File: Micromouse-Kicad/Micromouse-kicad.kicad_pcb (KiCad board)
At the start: 2 copper layers, 101 parts, among them J1 SWD, J2 USB_B_Micro, J3 UARTBTH, J4 Batería, J5 VL6180x, J6 MotorEncodL, J7 MotorEncodR, Q1 BS170, Q2 BS170, Q3 BS170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

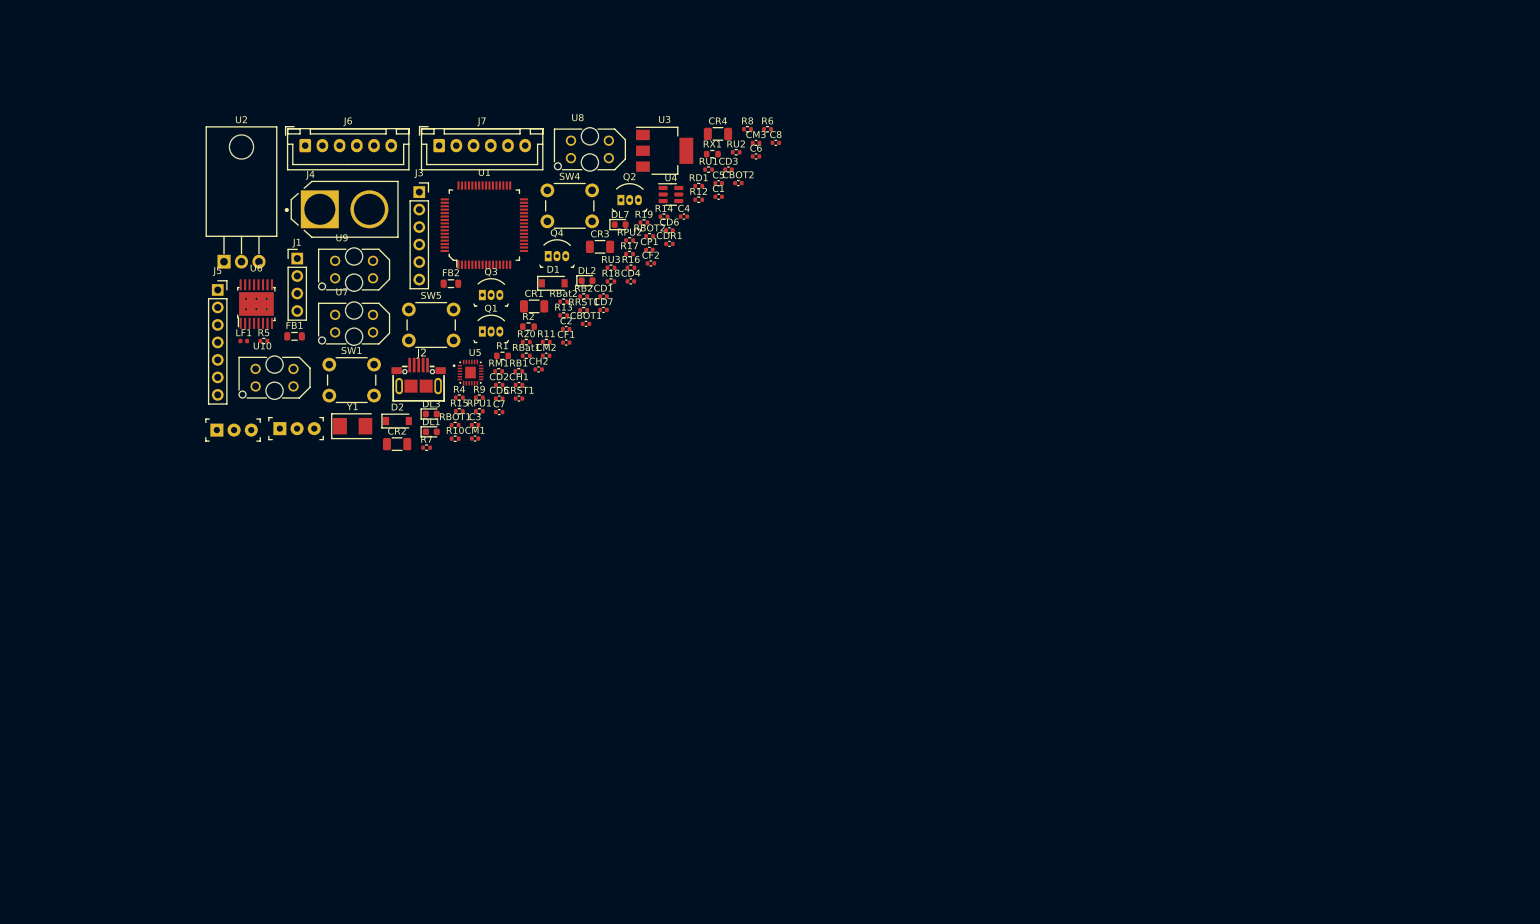
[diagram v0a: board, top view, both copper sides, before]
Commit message: Avance PCB - Forma y motores
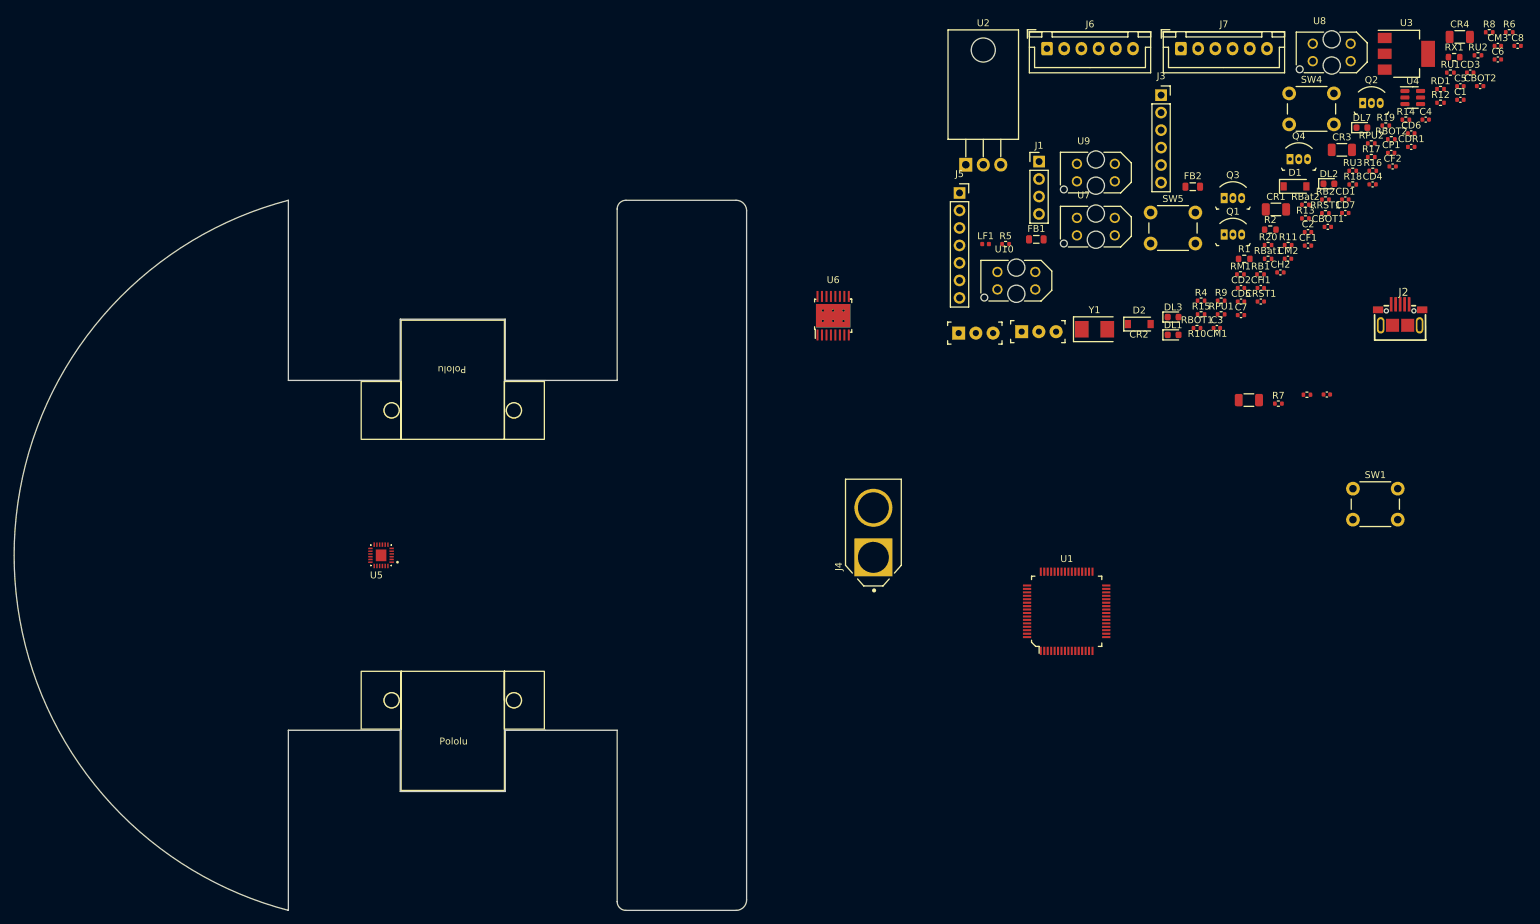
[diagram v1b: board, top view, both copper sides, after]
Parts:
- added Pololu: MotorHolder, custom:MotorHolder, F.Cu at (145.2, 119.5)
- added Pololu: MotorHolder, custom:MotorHolder, F.Cu at (160.2, 85.8)
- moved SW1 149.8 mm to (283.4, 92.9)
- moved J2 142.8 mm to (290.2, 67.7)
- moved CM1 123.9 mm to (279.6, 79.3)
- moved CR2 123.9 mm to (268.3, 80.1)
- moved R7 123.9 mm to (272.6, 80.6)
- moved R10 123.9 mm to (276.7, 79.3)
- moved D1 108.6 mm to (275.0, 49.0)
- moved R11 108.6 mm to (274.0, 57.6)
- moved C1 108.6 mm to (299.0, 36.5)
- moved C2 108.6 mm to (276.9, 55.7)
- moved C3 108.6 mm to (263.6, 69.6)
- moved C5 108.6 mm to (299.0, 34.5)
- moved C6 108.6 mm to (304.4, 30.6)
- moved C7 108.6 mm to (267.1, 67.7)
- moved C8 108.6 mm to (307.3, 28.6)
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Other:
- board outline added: 106.4 x 103.1 mm

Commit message: Motores routeados
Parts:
- RU2, RU3: footprint Resistor_SMD:R_0402_1005Metric -> Resistor_SMD:R_0603_1608Metric
- U2: value LM7805_TO220 -> AMS1117-5.0; footprint Package_TO_SOT_THT:TO-220-3_Horizontal_TabDown -> Package_TO_SOT_SMD:SOT-223-3_TabPin2
- moved C8 205.6 mm to (110.2, 87.4)
- moved C6 204.3 mm to (108.2, 87.4)
- moved R18 187.5 mm to (98.6, 80.8)
- moved R14 186.2 mm to (110.2, 83.8), turned to 180 degrees
- moved CR4 184.4 mm to (129.1, 99.3)
- moved U3 183.2 mm to (122.9, 102.2), turned to 90 degrees
- moved U7 181.2 mm to (67.3, 84.8), turned to 90 degrees
- moved R16 180.1 mm to (110.2, 85.1), turned to 180 degrees
- moved R1 179.2 mm to (90.1, 34.9)
- moved R11 179.2 mm to (96.4, 32.9)
- moved R12 179.2 mm to (118.6, 12.3)
- moved R13 179.2 mm to (98.9, 29.1)
- moved C1 179.2 mm to (121.4, 11.8)
- moved C2 179.2 mm to (99.3, 31.0)
- moved C3 179.2 mm to (86.1, 45.0)
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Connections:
- U2 pad 1: Net-(CR1-Pad1) -> GND
- U2 pad 2: GND -> +5V
- U2 pad 3: +5V -> Net-(CR1-Pad1)
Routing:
- net GND: track 0.00 -> 75.9 mm, vias 0 -> 29
- net TIM1_CH1: track 0.00 -> 44.5 mm, vias 0 -> 2
- net TIM1_CH2: track 0.00 -> 43.2 mm, vias 0 -> 2
- net TIM8_CH1: track 0.00 -> 40.5 mm, vias 0 -> 2
- net TIM8_CH2: track 0.00 -> 35.5 mm, vias 0 -> 2
- net MR1: track 0.00 -> 32.4 mm, vias 0 -> 2
- net MR2: track 0.00 -> 28.9 mm, vias 0 -> 2
- net +3.3V: track 0.00 -> 26.7 mm, vias 0 -> 9
- net ML1: track 0.00 -> 24.8 mm, vias 0 -> 2
- net ML2: track 0.00 -> 24.3 mm, vias 0 -> 2
- net +5V: track 0.00 -> 23.0 mm, vias 0 -> 4
- net OutMR2: track 0.00 -> 21.9 mm
- net /USB_STM32_D+: track 0.00 -> 19.1 mm
- net OutML2: track 0.00 -> 19.1 mm
- net /USB_STM32_D-: track 0.00 -> 17.3 mm
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- added copper zone on In2.Cu, net +3.3V
- added copper zone on In2.Cu, net +5V
- added copper zone on In1.Cu, net GND
- added copper zone on In2.Cu, net VCC
- added copper zone on In2.Cu, net Vdrive
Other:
- copper layers 2 -> 4

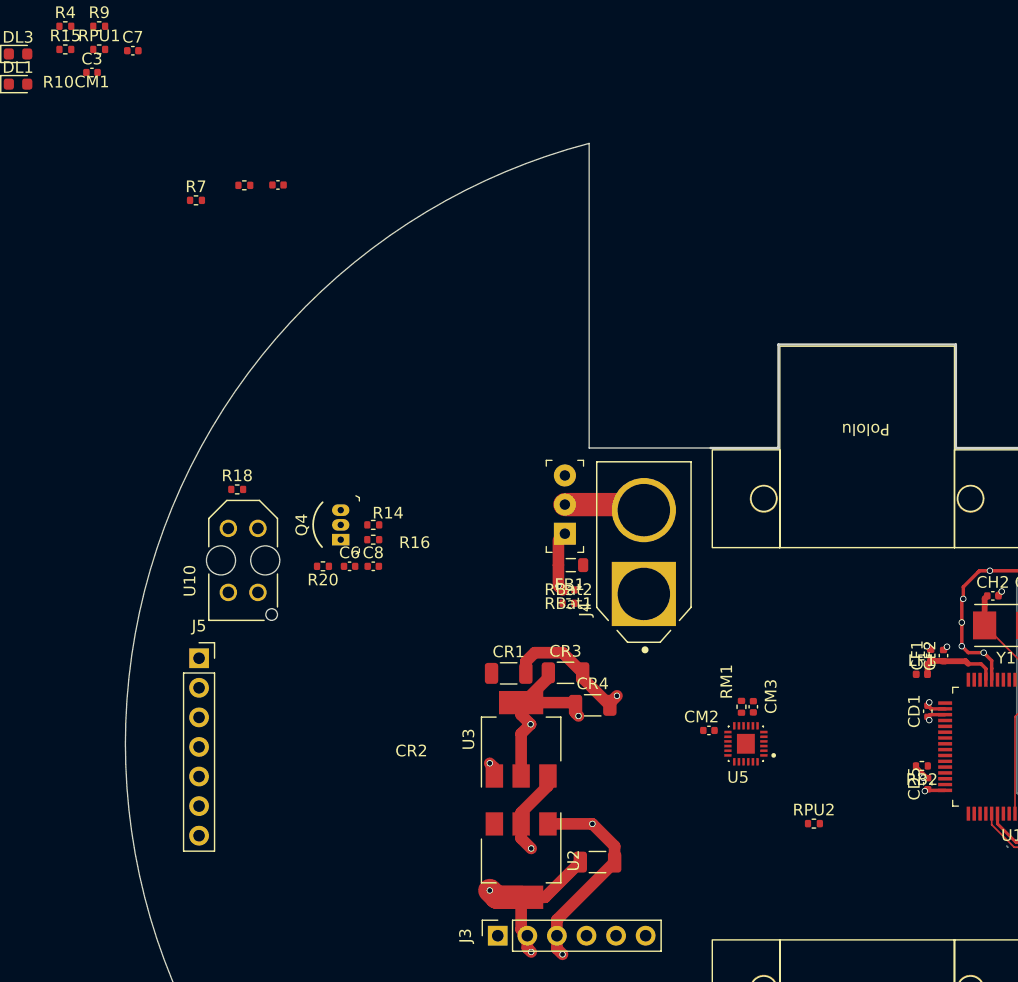
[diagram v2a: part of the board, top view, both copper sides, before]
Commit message: MPU6500 routeado
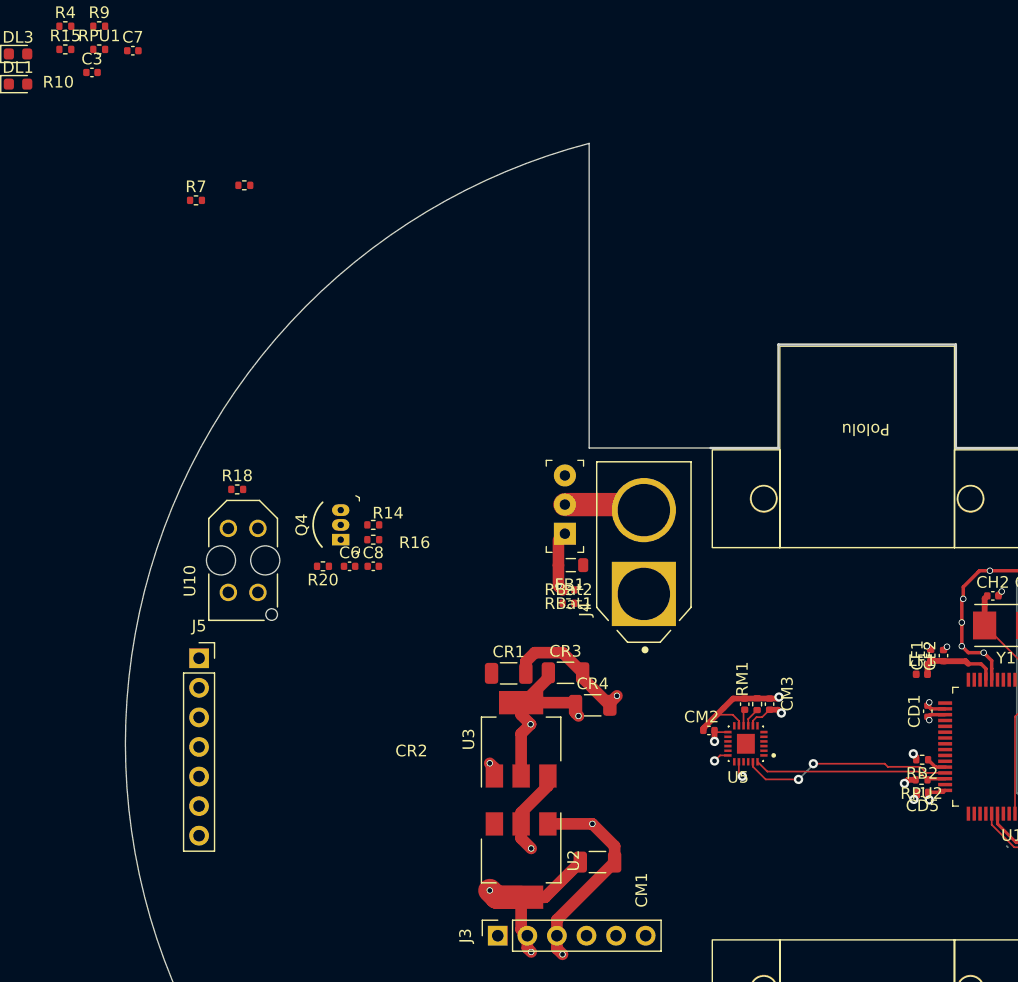
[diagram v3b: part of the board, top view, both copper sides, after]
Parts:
- moved CM1 60.0 mm to (142.1, 99.2), turned to 90 degrees
- moved RPU2 9.98 mm to (157.3, 105.7), turned to 180 degrees
- moved CM3 1.42 mm to (144.3, 99.2)
- moved RM1 1.37 mm to (143.2, 99.2)
- moved CD5 0.87 mm to (157.4, 106.8), turned to 180 degrees
- moved RB2 0.53 mm to (157.4, 104.0)
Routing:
- net I2C2_SCL: track 0.00 -> 18.3 mm, vias 0 -> 2
- net I2C2_SDA: track 0.00 -> 16.8 mm
- net GND: track 75.9 -> 88.6 mm, vias 29 -> 33
- net +3.3V: track 26.7 -> 33.7 mm, vias 9 -> 12
- net Net-(RB2-Pad1): track 0.00 -> 1.72 mm
- net Net-(RM1-Pad1): track 0.00 -> 1.67 mm
- net Net-(CM1-Pad1): track 0.00 -> 1.42 mm

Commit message: Casi todo routeado
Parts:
- R4: footprint Resistor_SMD:R_0402_1005Metric -> Resistor_SMD:R_0603_1608Metric
- moved DL3 183.5 mm to (252.3, 105.8), turned to 90 degrees
- moved R1 179.3 mm to (256.4, 101.7), turned to -90 degrees
- moved DL1 179.1 mm to (248.5, 105.8), turned to 90 degrees
- moved DL2 174.4 mm to (256.4, 105.8), turned to 90 degrees
- moved R2 173.6 mm to (252.2, 101.9), turned to -90 degrees
- moved RX1 160.1 mm to (248.5, 101.7), turned to -90 degrees
- moved U8 131.1 mm to (114.3, 135.5)
- moved R6 127.2 mm to (121.6, 129.0), turned to -90 degrees
- moved R8 127.0 mm to (122.9, 129.0), turned to -90 degrees
- moved R12 121.5 mm to (126.5, 133.5), turned to -90 degrees
- moved Q2 120.8 mm to (124.1, 132.0), turned to 180 degrees
- moved C4 115.0 mm to (126.5, 129.3), turned to 90 degrees
- moved C2 103.9 mm to (126.5, 131.3), turned to -90 degrees
- moved C1 102.7 mm to (114.1, 114.3), turned to 90 degrees
- moved R5 97.6 mm to (109.6, 113.9), turned to -90 degrees
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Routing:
- net FR_Reciever: track 0.00 -> 90.0 mm, vias 0 -> 2
- net L_Reciever: track 0.00 -> 82.9 mm, vias 0 -> 2
- net FL_Reciever: track 0.00 -> 66.6 mm, vias 0 -> 2
- net R_Reciever: track 0.00 -> 65.6 mm, vias 0 -> 2
- net FR_Emitter: track 0.00 -> 63.5 mm, vias 0 -> 2
- net R_Emitter: track 0.00 -> 60.6 mm, vias 0 -> 2
- net I2C2_SDA: track 16.8 -> 75.8 mm, vias 0 -> 3
- net UART4_RX: track 0.00 -> 54.9 mm, vias 0 -> 2
- net FL_Emitter: track 0.00 -> 54.7 mm, vias 0 -> 2
- net I2C2_SCL: track 18.3 -> 72.0 mm
- net +3.3V: track 33.7 -> 85.4 mm, vias 12 -> 24
- net UART4_TX: track 0.00 -> 49.9 mm
- net L_Emitter: track 0.00 -> 47.8 mm
- net GND: track 88.6 -> 136.1 mm, vias 33 -> 46
- net RST: track 0.00 -> 46.9 mm, vias 0 -> 2
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
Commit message: PCB Completa - Depurada
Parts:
- removed DL1: ROJO, LED_SMD:LED_0603_1608Metric
- removed DL3: VERDE, LED_SMD:LED_0603_1608Metric
- removed R2: 220, Resistor_SMD:R_0603_1608Metric
- removed RX1: 750, Resistor_SMD:R_0603_1608Metric
- moved R1 92.4 mm to (164.8, 113.3)
- moved DL2 92.3 mm to (164.8, 116.4)
- moved SW4 65.9 mm to (168.7, 84.5), turned to 45 degrees
- moved RBOT1 63.5 mm to (165.9, 86.0), turned to 45 degrees
- moved CBOT1 63.0 mm to (171.8, 83.5), turned to 45 degrees
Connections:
- U1 pad 39: LED1 -> unconnected-(U1-Pad39)
- U1 pad 43: LED6 -> unconnected-(U1-Pad43)
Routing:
- net Boton: track 0.00 -> 41.2 mm, vias 0 -> 1
- net unconnected-(J2-Pad6): track 0.00 -> 10.5 mm
- net +3.3V: track 85.4 -> 90.2 mm, vias 24 -> 27
- net LED5: track 0.00 -> 4.78 mm, vias 0 -> 2
- net GND: track 136.1 -> 138.1 mm, vias 46 -> 48
- net MR1: track 32.4 -> 34.2 mm
- net Net-(DL2-Pad2): track 0.00 -> 1.51 mm
- net Boton2: track 38.2 -> 39.5 mm
- net VDDA: track 7.22 -> 7.83 mm
- net UART4_RX: vias 2 -> 1
